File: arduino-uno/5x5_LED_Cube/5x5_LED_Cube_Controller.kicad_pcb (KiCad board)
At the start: 2 copper layers, 120.7 x 97.8 mm, 39 parts, among them J1 Arduino, J2 Power, J3 Layers, Q1 DMG2305UX, Q2 DMG2305UX, Q3 DMG2305UX, Q4 DMG2305UX, Q5 DMG2305UX, U1 TLC5940NT, U2 TLC5940NT

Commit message: Added traces for Arduino side
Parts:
- moved Q5 5.08 mm to (204.5, 115.6)
- moved J3 5.08 mm to (198.1, 100.9)
- moved Q1 5.08 mm to (204.5, 90.2)
- moved Q2 5.08 mm to (204.5, 96.5)
- moved Q3 5.08 mm to (204.2, 102.9)
- moved Q4 5.08 mm to (204.5, 109.2)
- moved J1 4.58 mm to (236.2, 74.9)
- moved J2 4.02 mm to (236.2, 85.1)
- moved R1 1.27 mm to (231.1, 61.0)
- moved R3 1.27 mm to (231.1, 57.6)
- moved U1 1.27 mm to (218.4, 41.9)
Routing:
- net GND: track 0.00 -> 103.4 mm, vias 0 -> 2
- net +5V: track 0.00 -> 97.3 mm, vias 0 -> 1
- net /ArduinoD10(BLANK): track 0.00 -> 59.9 mm
- net /ArduinoD3(GSCLK): track 0.00 -> 56.5 mm
- net /ArduinoD13(SCLK): track 0.00 -> 54.1 mm
- net /ArduinoD9(XLAT): track 0.60 -> 54.6 mm
- net /ArduinoD11(SIN): track 0.00 -> 32.1 mm
- net /SOUT1: track 0.00 -> 19.9 mm
- net /IREF1: track 0.00 -> 5.28 mm
- net /IREF2: track 0.00 -> 5.08 mm
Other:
- board outline removed

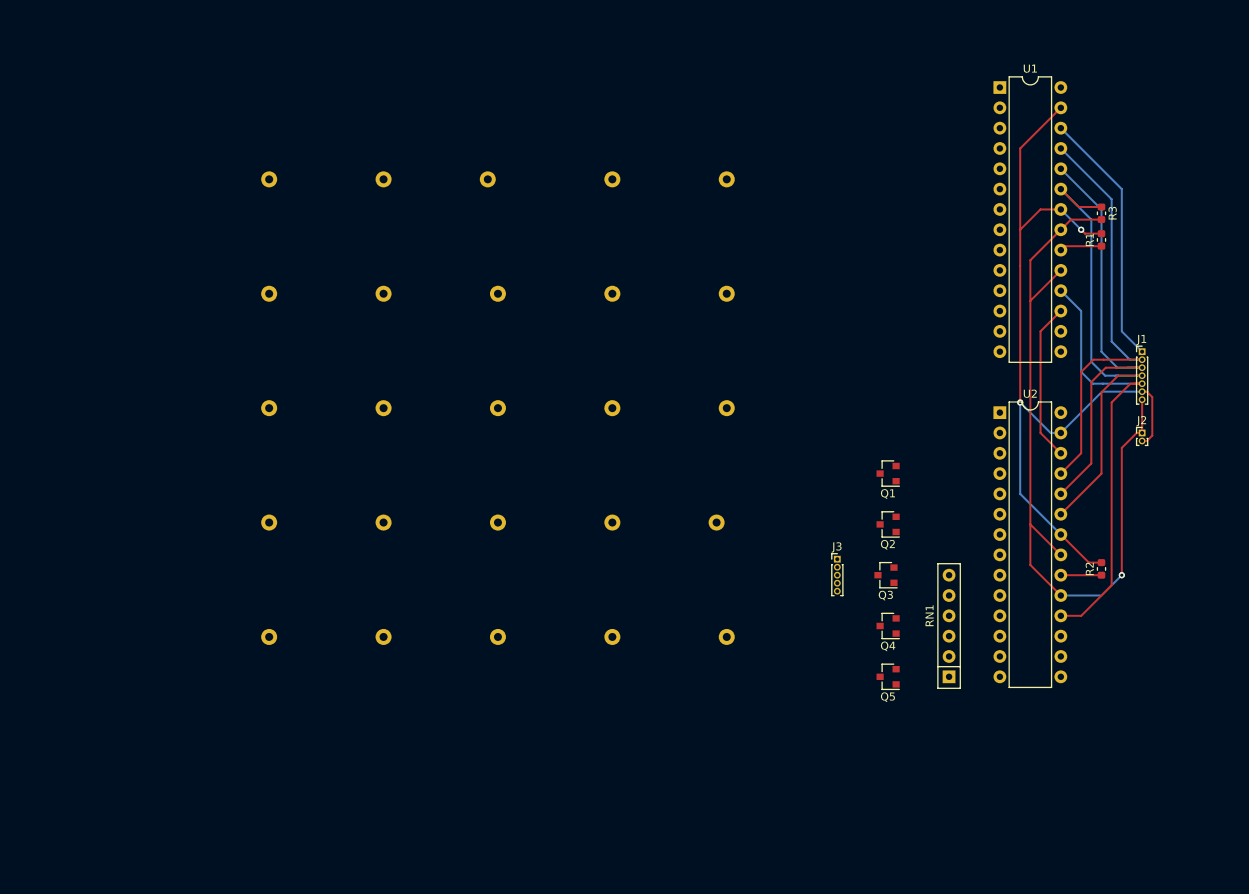
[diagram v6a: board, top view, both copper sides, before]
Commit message: PCB shrunken to the max
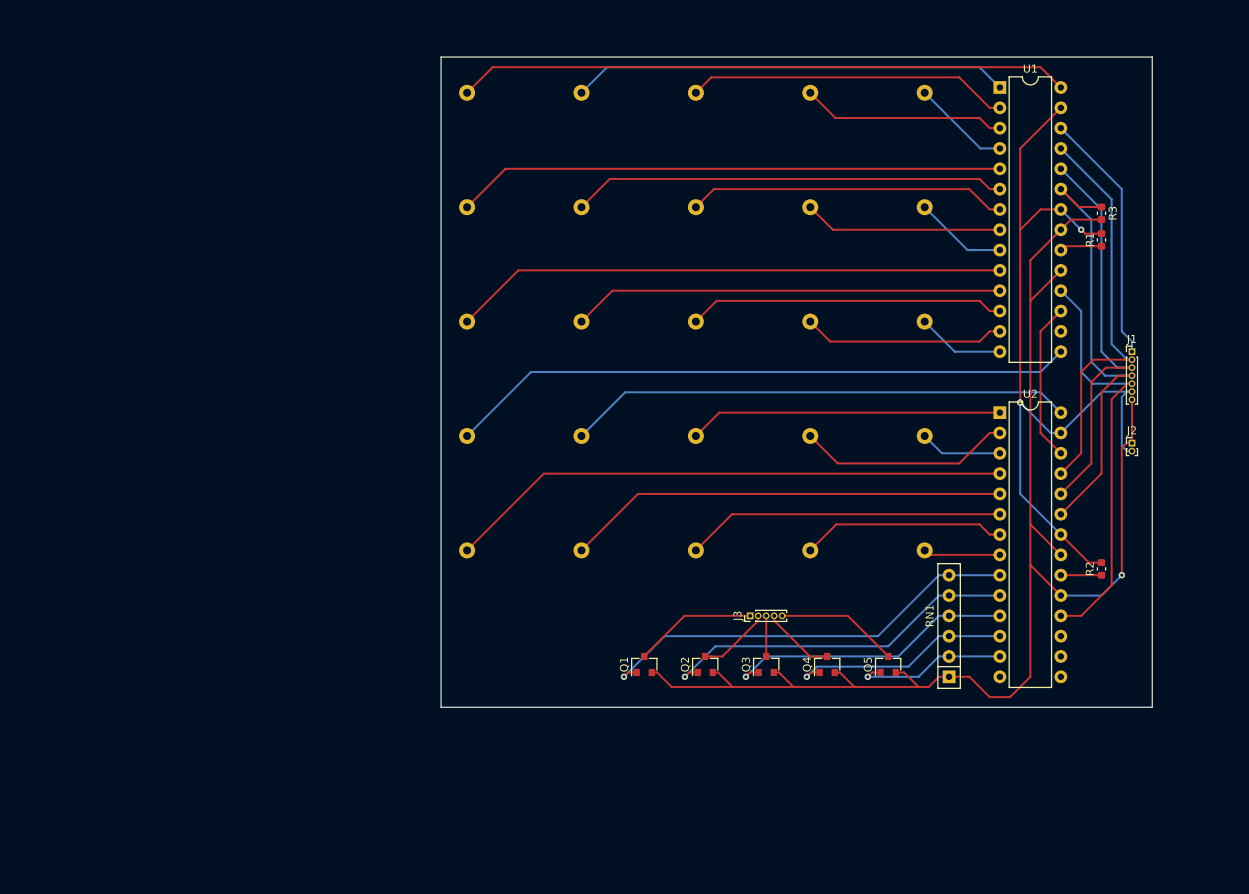
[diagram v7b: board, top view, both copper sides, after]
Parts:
- moved Q1 38.7 mm to (174.0, 114.0), turned to 90 degrees
- moved Q2 28.8 mm to (181.6, 114.0), turned to 90 degrees
- moved D20 28.2 mm to (209.0, 85.5)
- moved D3 28.2 mm to (180.4, 42.6)
- moved D1 27.0 mm to (151.8, 42.6)
- moved D16 27.0 mm to (151.8, 85.5)
- moved D18 27.0 mm to (180.4, 85.5)
- moved D19 27.0 mm to (194.7, 85.5)
- moved D21 27.0 mm to (151.8, 99.8)
- moved D23 27.0 mm to (180.4, 99.8)
- moved D24 27.0 mm to (194.7, 99.8)
- moved D4 27.0 mm to (194.7, 42.6)
- moved D6 27.0 mm to (151.8, 56.9)
- moved D8 27.0 mm to (180.4, 56.9)
- moved D9 27.0 mm to (194.7, 56.9)
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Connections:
- U1 pad 16: Net-(U1-Pad16) -> (no net)
- U2 pad 14: Net-(U2-Pad14) -> (no net)
- U2 pad 15: Net-(U2-Pad15) -> (no net)
- U2 pad 16: Net-(U2-Pad16) -> (no net)
- U2 pad 17: Net-(U2-Pad17) -> (no net)
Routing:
- net /LED16: track 0.00 -> 78.6 mm
- net +5V: track 97.3 -> 174.7 mm
- net /LED1: track 0.00 -> 76.6 mm
- net /LED21: track 0.00 -> 70.6 mm
- net /LED11: track 0.00 -> 69.3 mm
- net /LED6: track 0.00 -> 68.6 mm
- net /LED17: track 0.00 -> 63.2 mm
- net /LED22: track 0.00 -> 55.2 mm
- net /LED2: track 0.00 -> 54.7 mm
- net /LED7: track 0.00 -> 54.3 mm
- net /Layer1Gate: track 0.05 -> 54.1 mm, vias 0 -> 1
- net /LED12: track 0.00 -> 53.9 mm
- net /Layer2Gate: track 0.00 -> 45.4 mm, vias 0 -> 1
- net /LED3: track 0.00 -> 40.4 mm
- net /LED8: track 0.00 -> 40.0 mm
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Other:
- board outline added: 88.9 x 81.3 mm

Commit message: Finished PCB
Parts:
- added REF**: MountingHole_3.2mm_M3_Pad_Via, MountingHole:MountingHole_3.2mm_M3_Pad_Via, F.Cu at (179.3, 135.6)
- added REF**: MountingHole_3.2mm_M3_Pad_Via, MountingHole:MountingHole_3.2mm_M3_Pad_Via, F.Cu at (100.6, 135.6)
- added REF**: MountingHole_3.2mm_M3_Pad_Via, MountingHole:MountingHole_3.2mm_M3_Pad_Via, F.Cu at (179.3, 64.5)
- moved Q1 57.2 mm to (120.9, 135.4)
- moved Q2 57.2 mm to (128.5, 135.4)
- moved Q5 57.2 mm to (151.4, 135.4)
- moved RN1 57.2 mm to (159.0, 136.9)
- moved D14 57.2 mm to (141.7, 92.5)
- moved D19 57.2 mm to (141.7, 106.8)
- moved D24 57.2 mm to (141.7, 121.1)
- moved D4 57.2 mm to (141.7, 63.9)
- moved D6 57.2 mm to (98.8, 78.2)
- moved D8 57.2 mm to (127.4, 78.2)
- moved D9 57.2 mm to (141.7, 78.2)
- moved D1 57.2 mm to (98.8, 63.9)
- moved D10 57.2 mm to (156.0, 78.2)
- moved D11 57.2 mm to (98.8, 92.5)
- moved D12 57.2 mm to (113.1, 92.5)
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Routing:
- net GND: track 103.4 -> 6.82 mm, vias 2 -> 0
- net +5V: track 174.7 -> 177.2 mm
- added copper zone on B.Cu, net GND
- added copper zone on F.Cu, net GND
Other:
- board text added: "+"
- board text added: "-"
- board text added: "2.7K"
- board text added: "4.7K"
- board text added: "5x5 LED Cube Driver Board V1.0"
- board text added: "BLANK"
- board text added: "GSCLK"
- board text added: "PWR"
- board text added: "SCLK"
- board text added: "SIN"
- board text added: "XLAT"
